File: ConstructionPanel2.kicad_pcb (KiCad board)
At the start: 2 copper layers, 98 x 88 mm, 59 parts, among them J1 Conn_01x03_Male, J2 Conn_01x03_Male, Q1 Q_NMOS_GSD

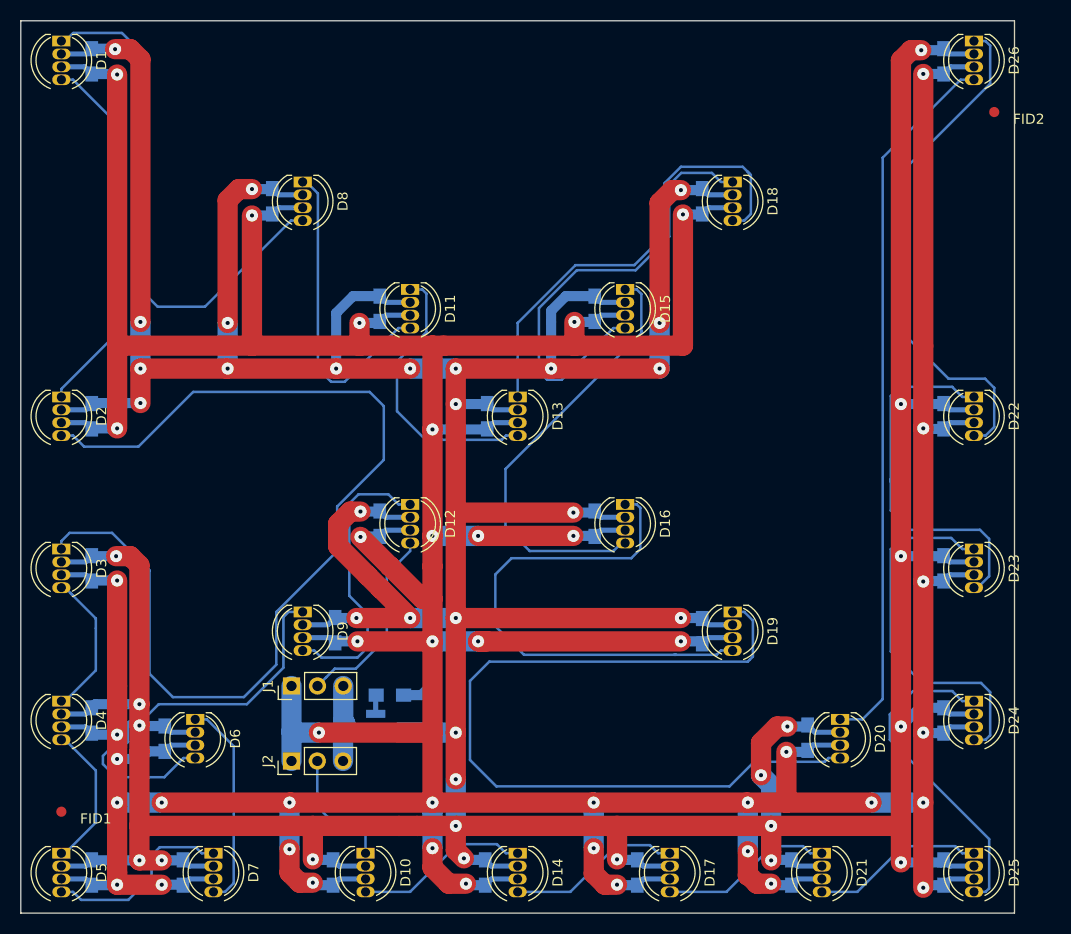
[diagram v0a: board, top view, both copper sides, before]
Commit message: change fiducial to 1.5
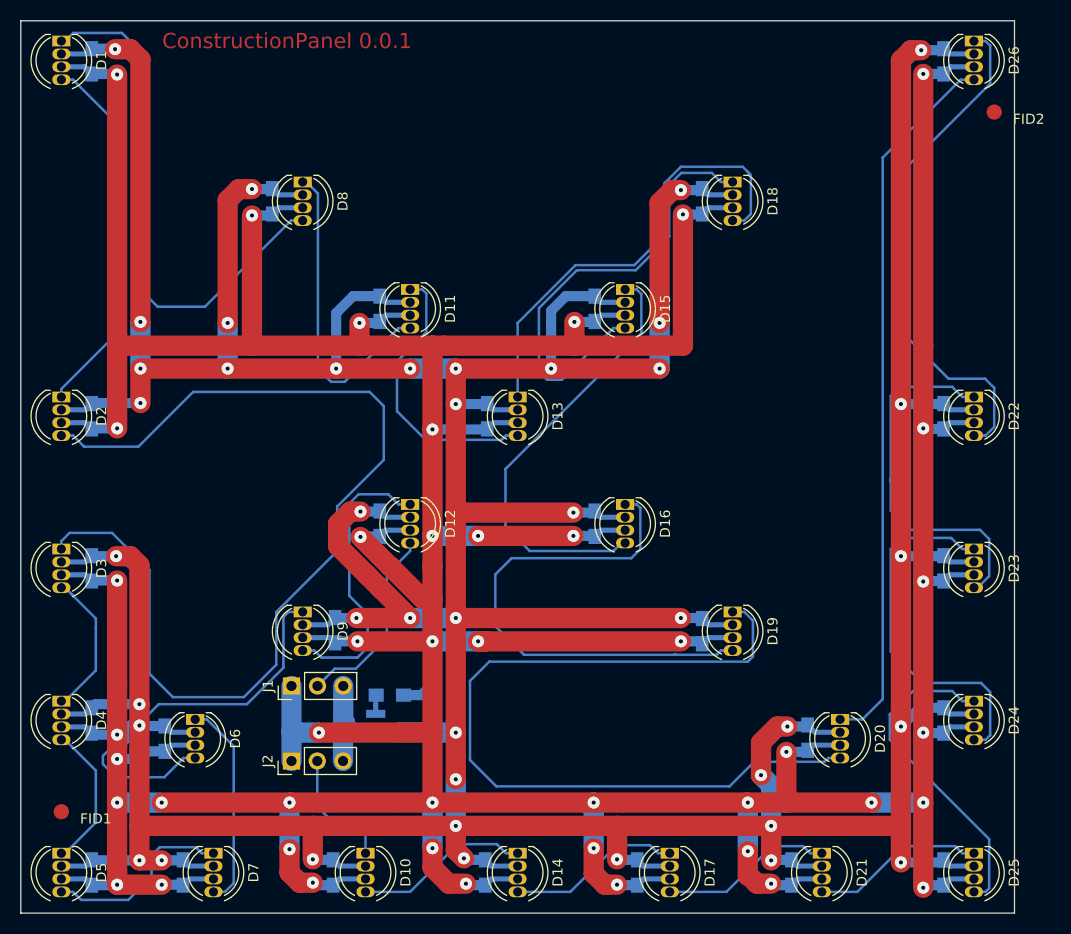
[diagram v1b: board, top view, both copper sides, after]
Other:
- board text added: "ConstructionPanel 0.0.1"
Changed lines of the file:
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@@
 (kicad_pcb (version 4) (host pcbnew 4.0.7)
   (general
-    (links 0)
+    (links 137)
     (no_connects 1)
-    (area 40.935238 44.800237 145.035 135.104762)
+    (area 33.061904 44.800237 158.938096 135.104762)
     (thickness 1.6)
-    (drawings 4)
+    (drawings 5)
     (tracks 725)
     (zones 0)
@@
     (mod_text_size 1 1)
     (mod_text_width 0.15)
-    (pad_size 1 1)
+    (pad_size 1.5 1.5)
     (pad_drill 0)
     (pad_to_mask_clearance 0.2)
@@
     (visible_elements FFFFFF7F)
     (pcbplotparams
-      (layerselection 0x00030_80000001)
+      (layerselection 0x01000_00000001)
       (usegerberextensions false)
       (excludeedgelayer true)
@@
       (padsonsilk false)
       (subtractmaskfromsilk false)
-      (outputformat 1)
-      (mirror false)
-      (drillshape 1)
+      (outputformat 4)
+      (mirror true)
+      (drillshape 0)
       (scaleselection 1)
       (outputdirectory ""))
@@
     )
     (fp_circle (center 0 0) (end 1.55 0) (layer F.CrtYd) (width 0.05))
-    (pad ~ smd circle (at 0 0) (size 1 1) (layers F.Cu F.Mask)
+    (pad ~ smd circle (at 0 0) (size 1.5 1.5) (layers F.Cu F.Mask)
       (solder_mask_margin 0.77) (clearance 0.77))
   )
@@
     )
     (fp_circle (center 0 0) (end 1.55 0) (layer F.CrtYd) (width 0.05))
-    (pad ~ smd circle (at 0 0) (size 1 1) (layers F.Cu F.Mask)
+    (pad ~ smd circle (at 0 0) (size 1.5 1.5) (layers F.Cu F.Mask)
       (solder_mask_margin 0.77) (clearance 0.77))
   )
-  (gr_line (start 46 46) (end 46 134) (layer Edge.Cuts) (width 0.01))
-  (gr_line (start 144 46) (end 46 46) (layer Edge.Cuts) (width 0.01))
-  (gr_line (start 144 134) (end 144 46) (layer Edge.Cuts) (width 0.01))
-  (gr_line (start 46 134) (end 144 134) (layer Edge.Cuts) (width 0.01))
+  (gr_text "ConstructionPanel 0.0.1" (at 72.25 48) (layer F.Cu)
+    (effects (font (size 1.5 1.5) (thickness 0.3)))
+  )
+  (gr_line (start 46 46) (end 46 134) (layer Edge.Cuts) (width 0.1))
+  (gr_line (start 144 46) (end 46 46) (layer Edge.Cuts) (width 0.1))
+  (gr_line (start 144 134) (end 144 46) (layer Edge.Cuts) (width 0.1))
+  (gr_line (start 46 134) (end 144 134) (layer Edge.Cuts) (width 0.1))
   (segment (start 72.7 116.1) (end 72.7 111.6) (width 2) (layer B.Cu) (net 1))
   (segment (start 72.7 119) (end 72.7 116.1) (width 2) (layer B.Cu) (net 1))

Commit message: via to 0.6 move connector
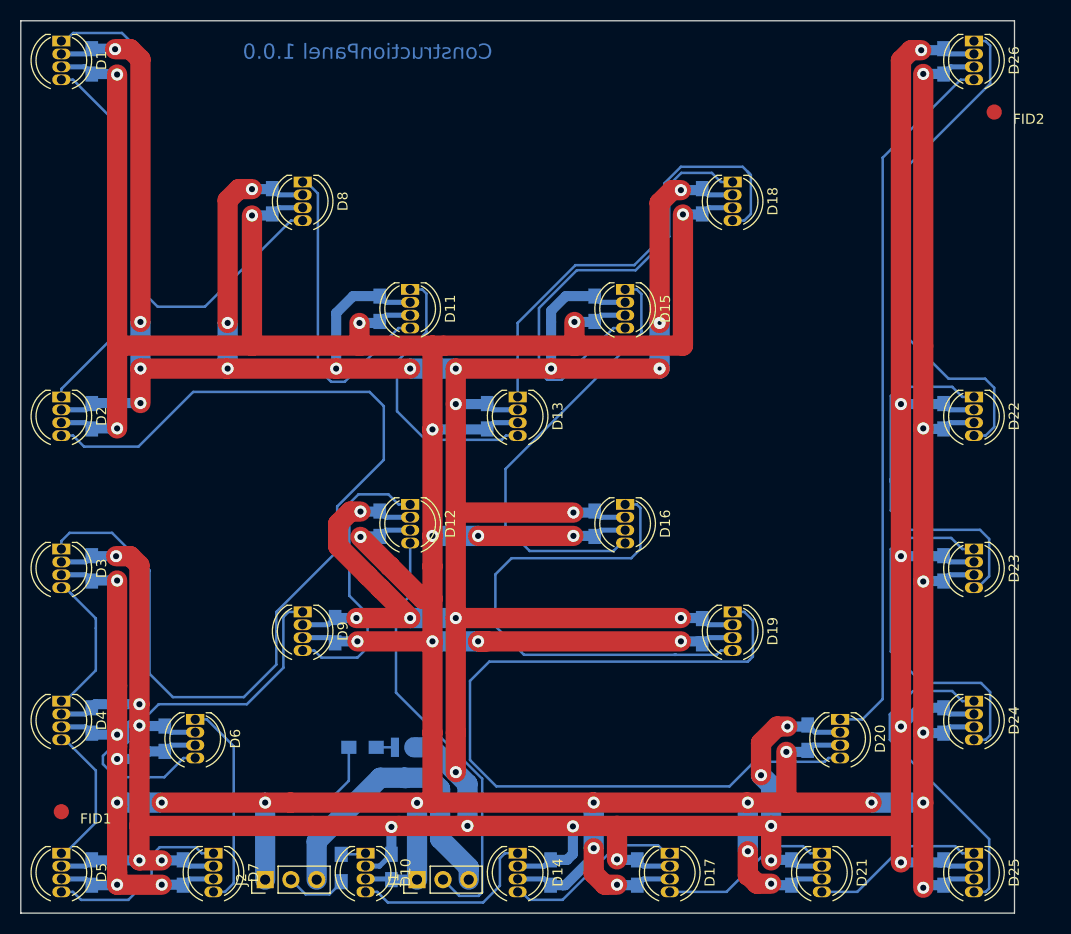
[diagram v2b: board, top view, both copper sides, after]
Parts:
- moved J1 22.8 mm to (85.1, 130.7)
- moved J2 12.0 mm to (70.1, 130.7)
- moved C7 6.45 mm to (98.2, 130.0)
- moved R2 5.81 mm to (79.7, 117.7), turned to 0 degrees
- moved Q1 5.81 mm to (83.8, 119.2), turned to 270 degrees
- moved C9 5.78 mm to (82.5, 129.4)
- moved R1 4.13 mm to (77.6, 129.6), turned to 90 degrees
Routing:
- net /DIN: track 19.1 -> 43.2 mm
- net Net-(J1-Pad3): track 7.57 -> 29.2 mm
- net +5V: track 638.5 -> 621.2 mm, vias 43 -> 38
- net GND: track 630.6 -> 624.7 mm, vias 41 -> 40
- net Net-(D10-Pad4): track 17.3 -> 19.0 mm
- net /DOUT: track 7.57 -> 6.14 mm
- net Net-(D14-Pad4): track 17.2 -> 17.9 mm
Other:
- board text added: "ConstructionPanel 1.0.0"
- board text removed: "ConstructionPanel 0.0.1"
